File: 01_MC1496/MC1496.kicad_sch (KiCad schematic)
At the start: 41 parts, among them J1 AudioJack2, J2 Screw_Terminal_01x03, J3 Screw_Terminal_01x02, U1 MC1496, U2 LM358, U3 SeeeduinoXIAO, U4 L7805

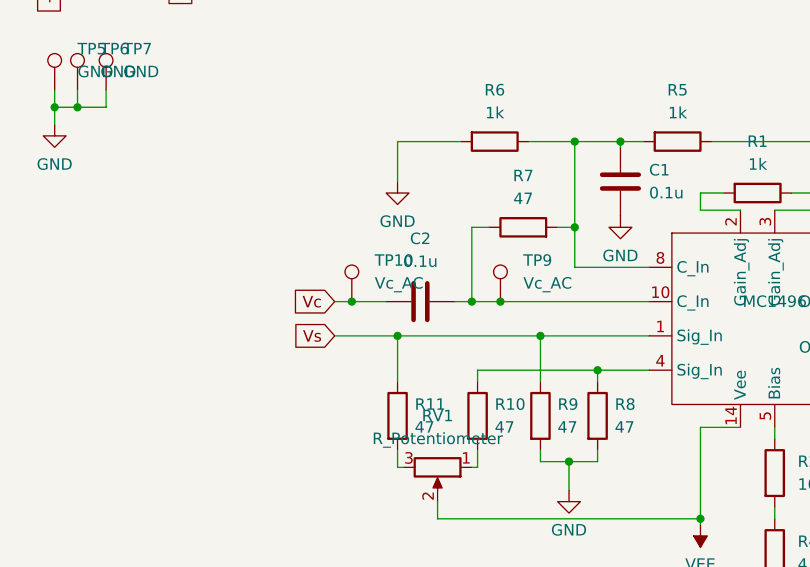
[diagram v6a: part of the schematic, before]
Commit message: TP名修正
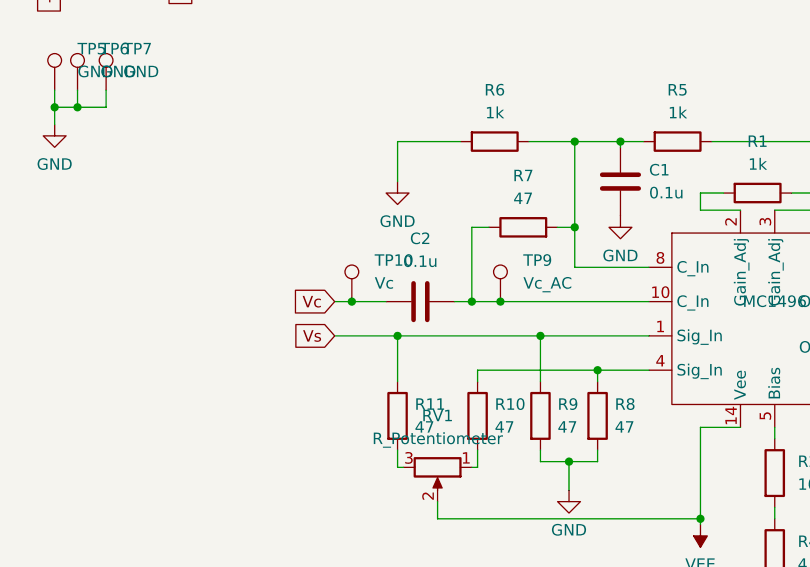
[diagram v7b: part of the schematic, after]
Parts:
- TP10: value Vc_AC -> Vc
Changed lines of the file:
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@@
       (effects (font (size 1.27 1.27)) (justify left))
     )
-    (property "Value" "Vc_AC" (at 107.95 89.408 0)
+    (property "Value" "Vc" (at 107.95 89.408 0)
       (effects (font (size 1.27 1.27)) (justify left))
     )

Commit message: 搬送波分圧調整
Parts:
- R14: value 4.7k -> 10k
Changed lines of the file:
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@@
       (effects (font (size 1.27 1.27)) (justify left))
     )
-    (property "Value" "4.7k" (at 204.47 97.155 0)
+    (property "Value" "10k" (at 204.47 97.155 0)
       (effects (font (size 1.27 1.27)) (justify left))
     )
